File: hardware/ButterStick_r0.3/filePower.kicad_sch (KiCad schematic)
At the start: 75 parts, among them U10 TPS62290, U6 TLV70025_SOT23-5, U7 TPS62290, U8 TPS62290, U9 TPS62290

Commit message: hw.r0d3: complete first pass of routing
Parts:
- removed C54, C57, C59, C62: 100nF, Capacitor_SMD:C_0402_1005Metric, symbol Device:C
- removed C55, C58, C60: 10nF, Capacitor_SMD:C_0402_1005Metric, symbol Device:C
- added J7: Conn_01x02_Male, Connector_PinHeader_2.54mm:PinHeader_1x02_P2.54mm_Vertical, symbol Connector:Conn_01x02_Male
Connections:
- net +5V: now also J7.1 (Pin_1)
- net GND: now also J7.2 (Pin_2)
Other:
- note added: "2.5V 20mA"
- moved on the sheet: C38, C39, C40, C41, C42, C43, C44, C45, C46, C47, C48, C49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

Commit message: hw.r0d3: Updated all DCDC supplies Added serdes power supplies
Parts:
- removed R55, R60: 10K, Resistor_SMD:R_0402_1005Metric, symbol Device:R
- removed U10, U7, U8, U9: TPS62290, Package_DFN_QFN:DFN-6-1EP_2x2mm_P0.65mm_EP1x1.6mm, symbol gkl_pmic:TPS62290
- removed U6: TLV70025_SOT23-5, Package_TO_SOT_SMD:SOT-23-5, symbol Regulator_Linear:TLV70025_SOT23-5
- added C29: 100nF, Capacitor_SMD:C_0402_1005Metric, symbol Device:C
- added C31: 1uF, Capacitor_SMD:C_0402_1005Metric, symbol Device:C
- added C54: 22pF, Capacitor_SMD:C_0402_1005Metric, symbol Device:C
- added C55: 4.7uF, Capacitor_SMD:C_0603_1608Metric, symbol Device:C
- added C57: 10uF, Capacitor_SMD:C_0603_1608Metric, symbol Device:C
- added L10: 2.2uH, Inductor_SMD:L_0805_2012Metric, symbol Device:L_Small
- added TP1: TestPoint_Small, TestPoint:TestPoint_Pad_D1.5mm, symbol Connector:TestPoint_Small
- added U10, U6, U7, U8, U9: TLV62569DRL, Package_TO_SOT_SMD:SOT-563, symbol Regulator_Switching:TLV62569DRL
- added U16, U17: TLV75712PDRV, Package_SON:WSON-6-1EP_2x2mm_P0.65mm_EP1x1.6mm, symbol Regulator_Linear:TLV75712PDRV
- C41: value 10nF -> 10uF; footprint Capacitor_SMD:C_0402_1005Metric -> Capacitor_SMD:C_0603_1608Metric; Mfg Samsung Electro-Mechanics -> (none); PN CL05B103KP5NNNC -> CL10A106MP8NNNC; SN-DK 1276-1002-1-ND -> 445-7486-1-ND
- R58: value 10K -> 53.6K
- R59: value 10K -> 13.0K
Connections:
- net +1V1: now also C81.1, C84.1, C87.1, L6.2, R65.2, TP8.1
- net +2V5: now also R58.2, C31.1, C54.1, C55.1, L10.2, TP1.1, U16.4 (EN), U16.6 (IN), U17.4 (EN), U17.6 (IN); no longer C41.1
- net +3V3: now also C79.1, C82.1, C85.1, L4.2, R61.2, TP6.1
- net +5V: now also C29.1, U10.3 (VIN), U10.5 (EN), U6.3 (VIN), U6.5 (EN), U7.3 (VIN), U7.5 (EN), U8.3 (VIN), U8.5 (EN), U9.3 (VIN), U9.5 (EN)
- net GND: now also C29.2, C31.2, C55.2, C57.2, U10.2 (GND), U16.3 (GND), U16.7 (GND), U17.3 (GND), U17.7 (GND), U6.2 (GND), U7.2 (GND), U8.2 (GND), U9.2 (GND); no longer R58.1
- net at L3.1: now also U7.4 (SW)
- net P_1.35_DRAM: now reaches C73.1, C74.1, C75.1, L3.2, R56.2, TP5.1
- net at R59.2: now also R58.1, C54.2, U6.1 (FB)
- net at C81.2, R65.1, R66.2: now also U10.1 (FB)
- net at L6.1: now also U10.4 (SW)
- net at C80.2, R63.1, R64.2: now also U9.1 (FB)
- net at L4.1: now also U8.4 (SW)
- net at C73.2, R56.1, R57.2: now also U7.1 (FB)
- net at C79.2, R61.1, R62.2: now also U8.1 (FB)
- net +1V2: now reaches C80.1, C83.1, C86.1, L5.2, R63.2, TP7.1
- net at L5.1: now also U9.4 (SW)
- new net: L10.1, U6.4 (SW)
- new net P_1V2_A: C41.1, U16.1 (OUT)
- new net P_1V2_T: C57.1, U17.1 (OUT)
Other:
- note added: "2.5V 20mA + Supplies VCCTX/VCCRK"
- note added: "Test Point 2v5"
- note removed: "2.5V 20mA"
- moved on the sheet: C38, C39, C40, C42, C44, C46, C48, C50, C61, C65, C68, C69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

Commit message: hw.r0d3: Tweaking routing
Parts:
- removed C64: 100nF, Capacitor_SMD:C_0402_1005Metric, symbol Device:C
- removed C69: 10uF, Capacitor_SMD:C_0603_1608Metric, symbol Device:C
- removed U16, U17: TLV75712PDRV, Package_SON:WSON-6-1EP_2x2mm_P0.65mm_EP1x1.6mm, symbol Regulator_Linear:TLV75712PDRV
- added C143: 1uF, Capacitor_SMD:C_0402_1005Metric, symbol Device:C
- added C144: 100nF, Capacitor_SMD:C_0402_1005Metric, symbol Device:C
- added Q4: Q_PMOS_GSD, Package_TO_SOT_SMD:SOT-23, symbol Device:Q_PMOS_GSD
- added Q5: Q_NMOS_GSD, Package_TO_SOT_SMD:SOT-23, symbol Device:Q_NMOS_GSD
- added R60, R73, R74, R90: 13.0K, Resistor_SMD:R_0402_1005Metric, symbol Device:R
- added R91, R92: 53.6K, Resistor_SMD:R_0402_1005Metric, symbol Device:R
- added U16, U17: TLV75801PDRV, Package_SON:WSON-6-1EP_2x2mm_P0.65mm_EP1x1.6mm, symbol Regulator_Linear:TLV75801PDRV
- added U18: TLV6001DCK, Package_TO_SOT_SMD:SOT-353_SC-70-5, symbol Amplifier_Operational:TLV6001DCK
- added U19: LM74700, Package_TO_SOT_SMD:SOT-23-6, symbol Power_Management:LM74700
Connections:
- net +2V5: now also U16.4 (EN), U16.6 (IN), U17.4 (EN), U17.6 (IN)
- net +3V3: now also U18.3 (-), U18.5 (V+)
- net +5V: now also Q4.2 (S), Q5.3 (D), U19.4 (CATHODE); no longer J7.1 (Pin_1)
- net GND: now also C143.2, R73.1, R90.1, R92.1, U16.3 (GND), U16.7 (GND), U17.3 (GND), U17.7 (GND), U18.2 (V-), U19.2 (GND)
- net P_1V2_A: now also R60.2, U16.1 (OUT)
- net P_1V2_T: now also R74.2, U17.1 (OUT)
- new net: C143.1, C144.1, J7.1 (Pin_1), Q5.2 (S), R91.2, U19.3 (EN), U19.6 (ANODE)
- new net: Q4.1 (G), U18.4
- new net: R91.1, R92.2, U18.1 (+)
- new net: R74.1, R90.2, U17.2 (FB)
- new net: R60.1, R73.2, U16.2 (FB)
- new net: Q5.1 (G), U19.5 (GATE)
- new net: C144.2, U19.1 (VCAP)
- new net VBUS_USB: Q4.3 (D)
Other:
- moved on the sheet: C29, C31, C38, C39, C40, C41, C42, C44, C46, C48, C50, C54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

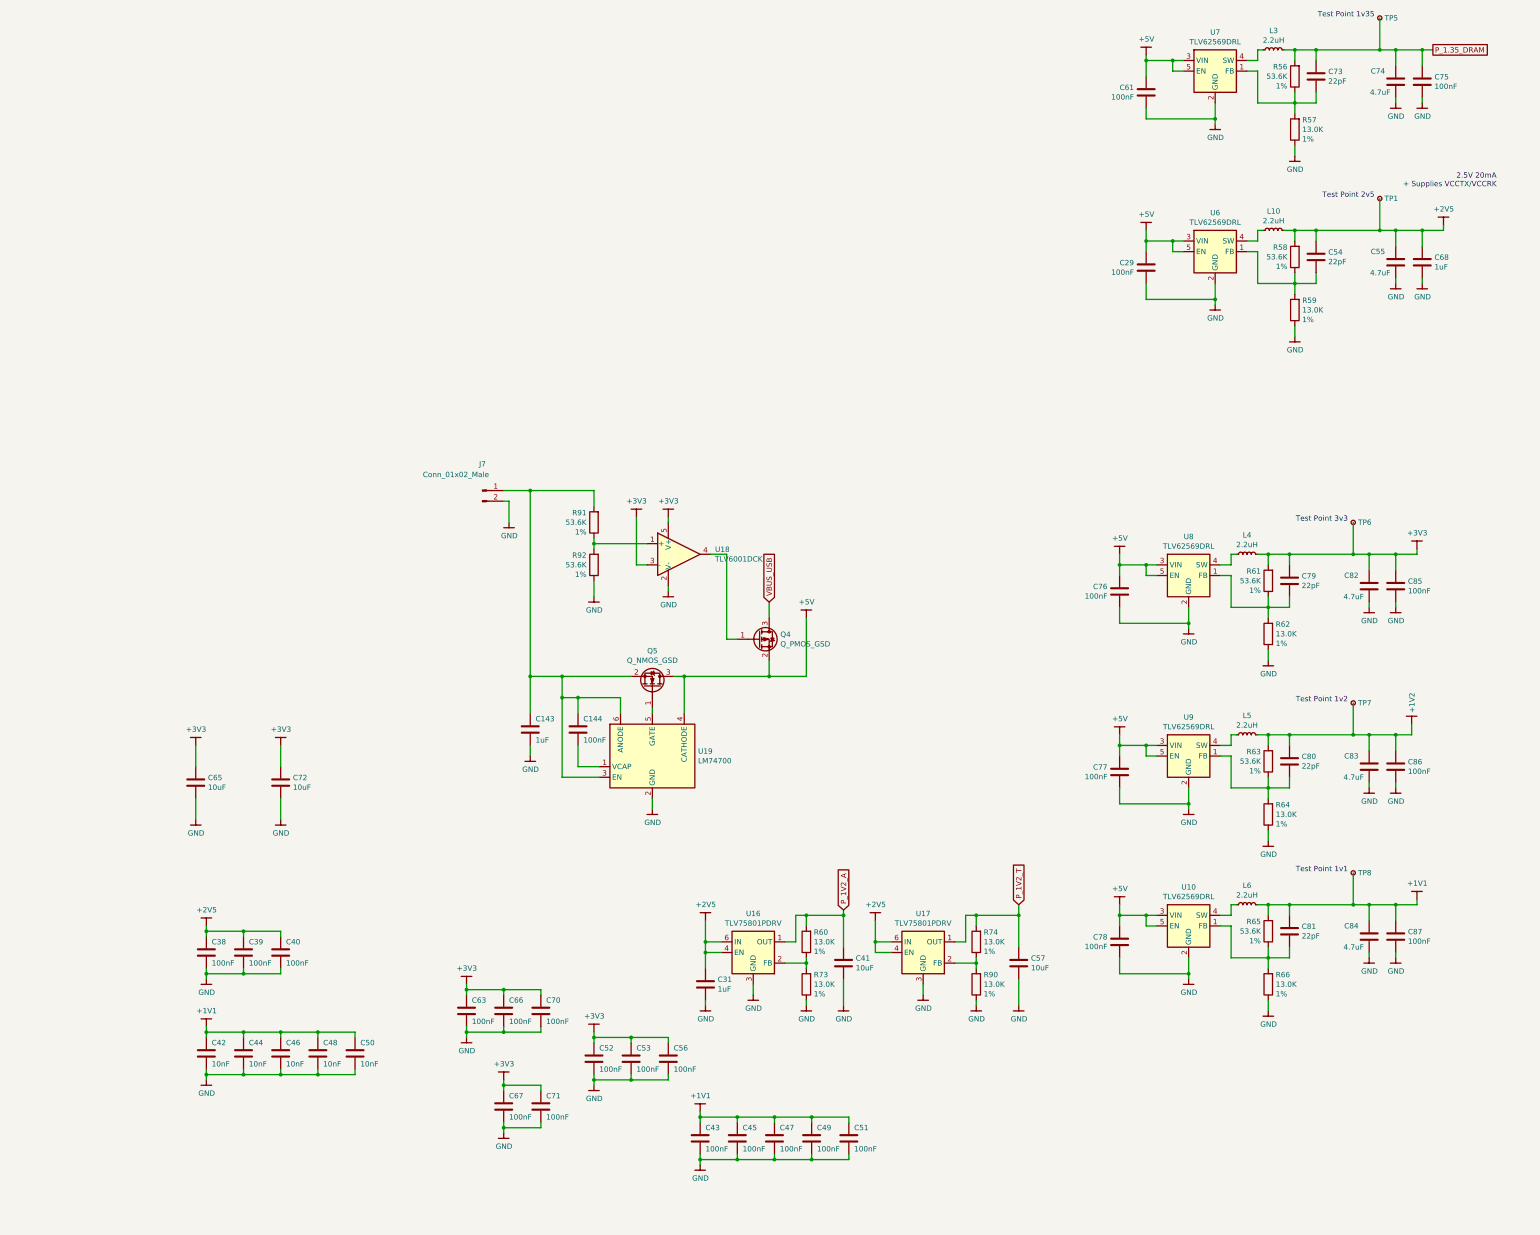
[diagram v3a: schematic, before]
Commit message: hw.r0d3: Small routing tweaks
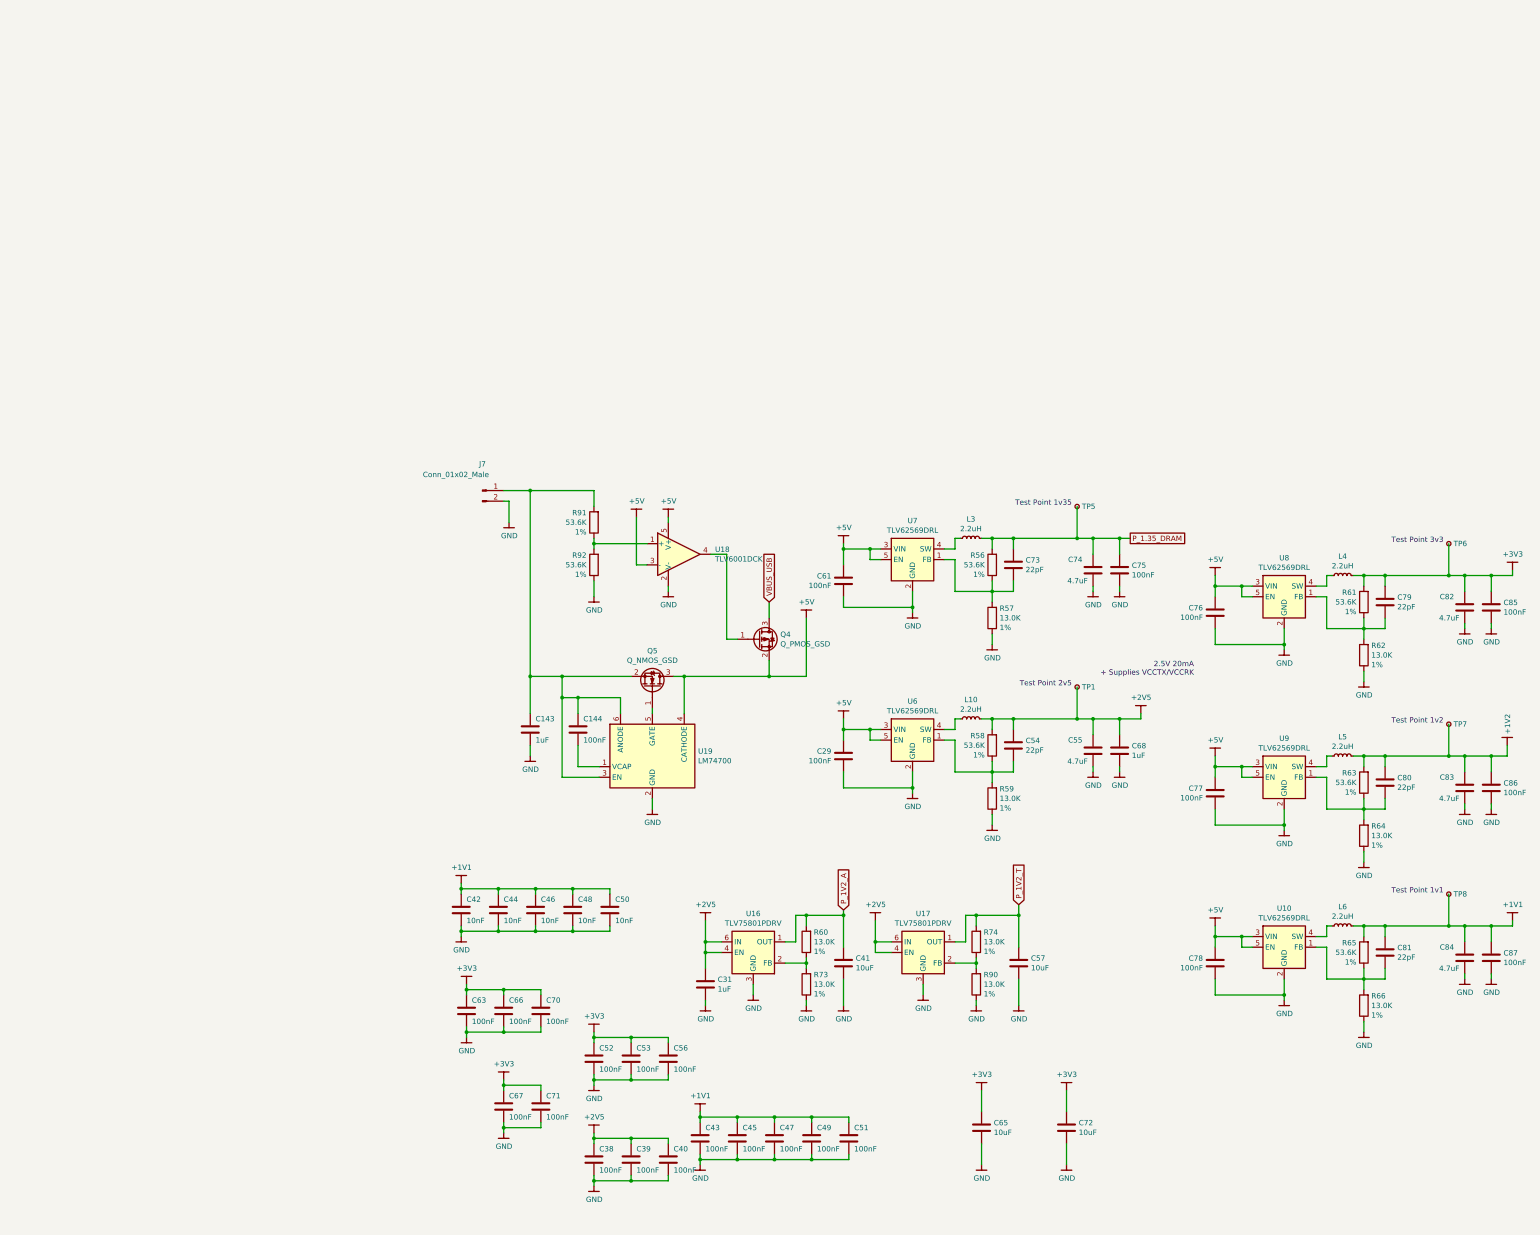
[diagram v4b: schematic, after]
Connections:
- net +3V3: no longer U18.3 (-), U18.5 (V+)
- net +5V: now also U18.3 (-), U18.5 (V+)
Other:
- moved on the sheet: C29, C38, C39, C40, C42, C44, C46, C48, C50, C54, C55, C61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

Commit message: hw.r0d3: Update schematic bus routing
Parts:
- removed C38, C39, C40, C43, C45, C47, C49, C51, C52, C53, C56, C63, C66, C67, C70, C71: 100nF, Capacitor_SMD:C_0402_1005Metric, symbol Device:C
- removed C42, C44, C46, C48, C50: 10nF, Capacitor_SMD:C_0402_1005Metric, symbol Device:C
- removed C65, C72: 10uF, Capacitor_SMD:C_0603_1608Metric, symbol Device:C
- C144, C29, C61, C75, C76, C77, C78, C85, C86, C87: value 100nF -> 0.1uF
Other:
- moved on the sheet: Q4
